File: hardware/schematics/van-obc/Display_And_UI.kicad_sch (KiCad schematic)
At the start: 8 parts, among them J1 J_LCD, J2 J_ENCODER, J3 J_BUZZER, J4 J_LEDS, Q2 BC107

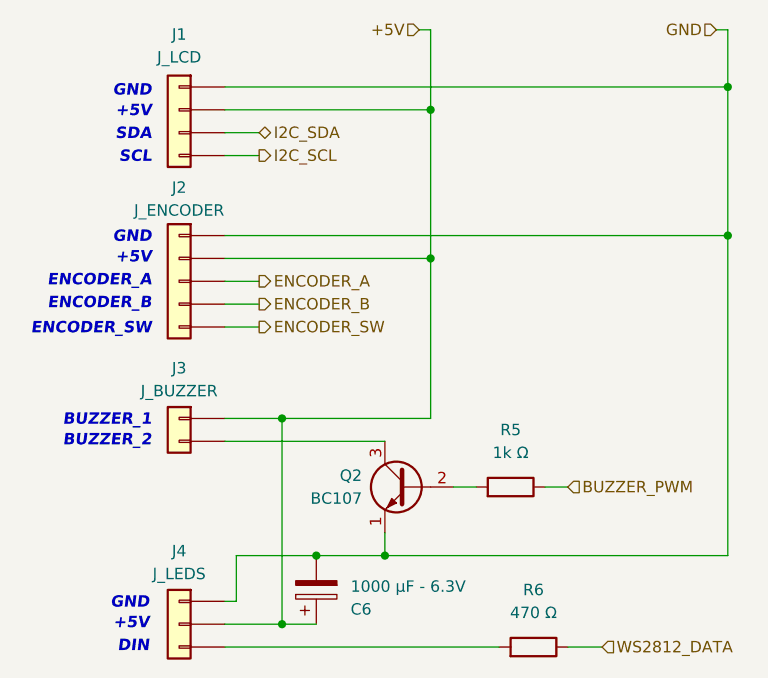
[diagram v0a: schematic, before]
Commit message: fix(tests): Corrections majeures KY040, BME280, MPU6050
- KY040 v2.1.0: Fix comptage + anti-rebond capacitif
- BME280 v1.0.1: Fix begin() avec &Wire
- MPU6050 v2.0.0: Simplification (acc only, dérive <2°)
- Ajout diagnostic_bme280.ino + CHANGELOG

Tests: 6/11 validés (55%)
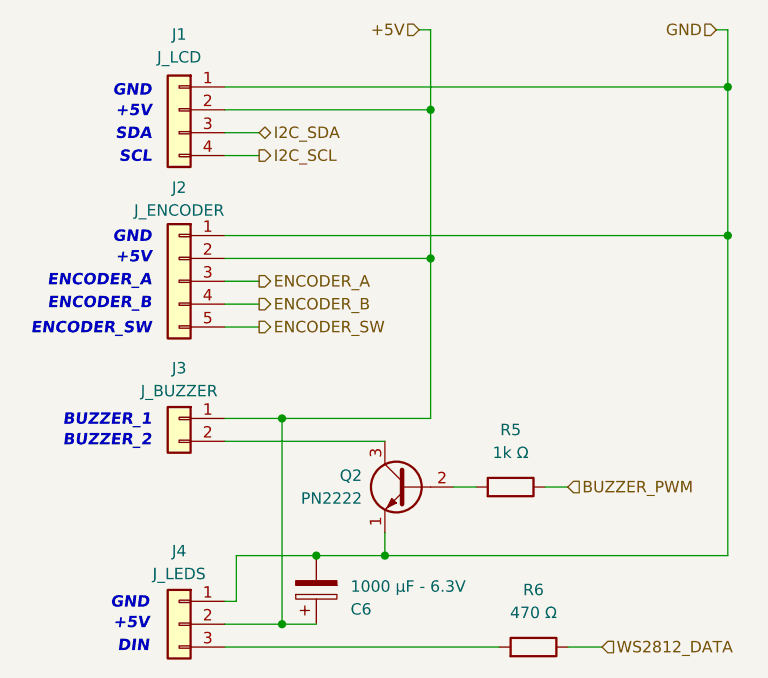
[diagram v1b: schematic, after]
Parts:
- C6: footprint (none) -> Capacitor_THT:CP_Radial_D8.0mm_P3.50mm
- J1: footprint (none) -> Connector_PinHeader_2.54mm:PinHeader_1x04_P2.54mm_Vertical
- J2: footprint (none) -> Connector_PinHeader_2.54mm:PinHeader_1x05_P2.54mm_Vertical
- J3: footprint (none) -> Connector_PinHeader_2.54mm:PinHeader_1x02_P2.54mm_Vertical
- J4: footprint (none) -> Connector_PinHeader_2.54mm:PinHeader_1x03_P2.54mm_Vertical
- Q2: value BC107 -> PN2222; footprint Package_TO_SOT_THT:TO-18-3 -> Package_TO_SOT_THT:TO-92_Inline; symbol Transistor_BJT:BC107 -> Transistor_BJT:PN2222A
- R5, R6: footprint (none) -> Resistor_THT:R_Axial_DIN0207_L6.3mm_D2.5mm_P10.16mm_Horizontal
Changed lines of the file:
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@@
 	(title_block
 		(title "Van Onboard Computer")
-		(date "2025-11-30")
-		(rev "1.0")
+		(date "2025-12-02")
+		(rev "1.1")
 	)
 	(text "GND"
@@
 			)
 		)
-		(property "Footprint" ""
+		(property "Footprint" "Connector_PinHeader_2.54mm:PinHeader_1x03_P2.54mm_Vertical"
 			(at 59.69 97.79 0)
 			(effects
@@
 			)
 		)
-		(property "Footprint" ""
+		(property "Footprint" "Connector_PinHeader_2.54mm:PinHeader_1x04_P2.54mm_Vertical"
 			(at 59.69 40.64 0)
 			(effects
@@
 			)
 		)
-		(property "Footprint" ""
+		(property "Footprint" "Connector_PinHeader_2.54mm:PinHeader_1x02_P2.54mm_Vertical"
 			(at 59.69 74.93 0)
 			(effects
@@
 			)
 		)
-		(property "Footprint" ""
+		(property "Footprint" "Resistor_THT:R_Axial_DIN0207_L6.3mm_D2.5mm_P10.16mm_Horizontal"
 			(at 96.52 84.328 90)
 			(effects
@@
 			)
 		)
-		(property "Footprint" ""
+		(property "Footprint" "Capacitor_THT:CP_Radial_D8.0mm_P3.50mm"
 			(at 75.8952 90.17 0)
 			(effects
@@
 			)
 		)
-		(property "Footprint" ""
+		(property "Footprint" "Resistor_THT:R_Axial_DIN0207_L6.3mm_D2.5mm_P10.16mm_Horizontal"
 			(at 99.06 102.108 90)
 			(effects
@@
 			)
 		)
-		(property "Footprint" ""
+		(property "Footprint" "Connector_PinHeader_2.54mm:PinHeader_1x05_P2.54mm_Vertical"
 			(at 59.69 59.69 0)
 			(effects
@@
 	)
 	(symbol
-		(lib_id "Transistor_BJT:BC107")
+		(lib_id "Transistor_BJT:PN2222A")
 		(at 85.09 82.55 0)
 		(mirror y)
@@
 			)
 		)
-		(property "Value" "BC107"
+		(property "Value" "PN2222"
 			(at 80.01 83.8199 0)
 			(effects
@@
 			)
 		)
-		(property "Footprint" "Package_TO_SOT_THT:TO-18-3"
+		(property "Footprint" "Package_TO_SOT_THT:TO-92_Inline"
 			(at 80.01 84.455 0)
 			(effects
@@
 			)
 		)
-		(property "Datasheet" "http://www.b-kainka.de/Daten/Transistor/BC108.pdf"
+		(property "Datasheet" "https://www.onsemi.com/pub/Collateral/PN2222-D.PDF"
 			(at 85.09 82.55 0)
 			(effects
@@
 			)
 		)
-		(property "Description" "0.1A Ic, 50V Vce, Low Noise General Purpose NPN Transistor, TO-18"
+		(property "Description" "1A Ic, 40V Vce, NPN Transistor, General Purpose Transistor, TO-92"
 			(at 85.09 82.55 0)
 			(effects
